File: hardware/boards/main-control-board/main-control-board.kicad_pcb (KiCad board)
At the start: 2 copper layers, 129 x 33 mm, 5 parts

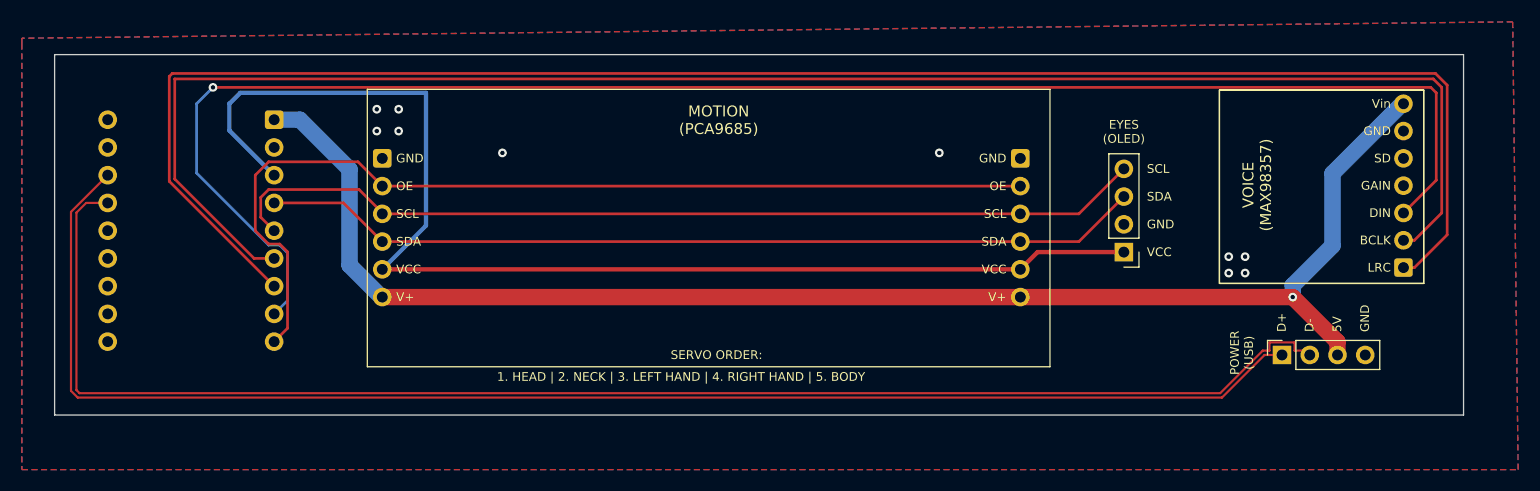
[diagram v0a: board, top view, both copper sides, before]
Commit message: feat(pcb): compact main control board layout and properties
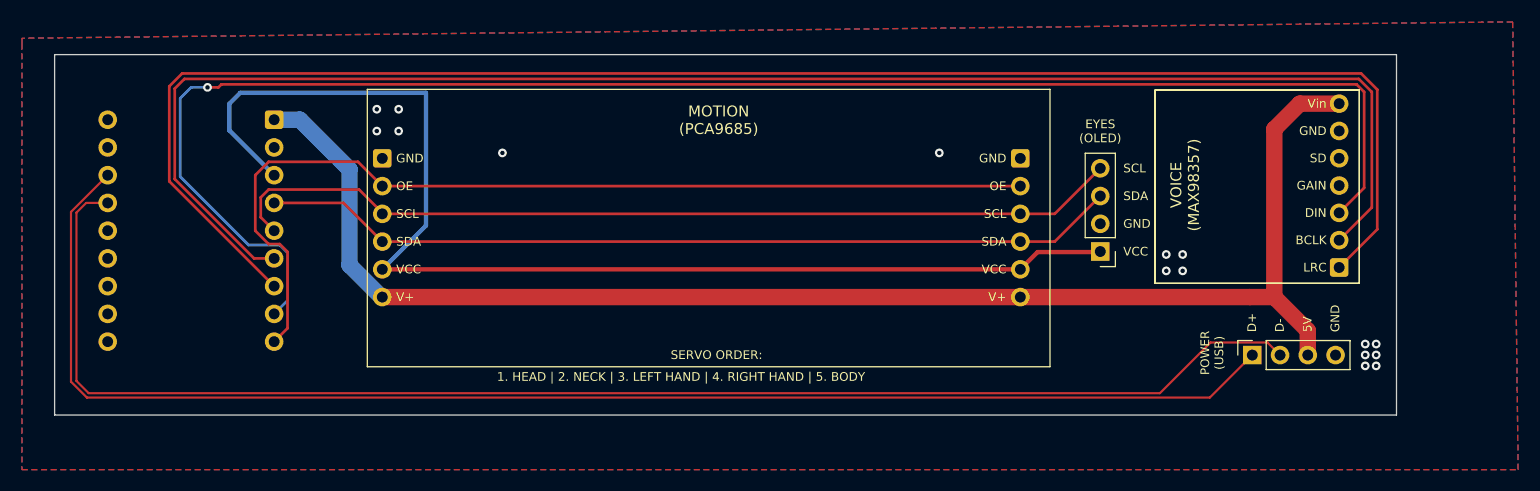
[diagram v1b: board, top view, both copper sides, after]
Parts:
- moved MAX1 5.89 mm to (233.6, 42.0)
- moved USB1 2.72 mm to (233.2, 57.5)
- moved OLED1 2.16 mm to (219.2, 48.0)
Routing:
- net /I2S_LRC: track 159.7 -> 151.7 mm
- net /I2S_BCLK: track 153.6 -> 145.7 mm
- net /USB_D-: track 135.8 -> 131.7 mm
- net /USB_D+: track 133.9 -> 130.7 mm
- net /I2S_DIN: track 150.4 -> 147.2 mm
- net /I2C_SDA: track 81.0 -> 78.8 mm
- net /I2C_SCL: track 85.5 -> 83.4 mm
- net +3.3V: track 113.0 -> 110.9 mm
- net +5V: track 134.0 -> 132.4 mm, vias 1 -> 0
- net GND: vias 10 -> 16
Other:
- board size 129 x 33 mm -> 122.9 x 33 mm

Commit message: prep PCB assembly
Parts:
- MAX1: value MAX98357 -> MAX98357A
- OLED1: value OLED -> Waveshare 0.91 OLED
- PCA1: value PCA9685 -> Adafruit PCA9685
- USB1: value USB -> Conn_01x04_Socket
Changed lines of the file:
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@@
 			)
 		)
-		(property "Value" "PCA9685"
+		(property "Value" "Adafruit PCA9685"
 			(at 0 1 0)
 			(unlocked yes)
@@
 		(sheetname "/")
 		(sheetfile "main-control-board.kicad_sch")
-		(attr through_hole)
+		(units
+			(unit
+				(name "A")
+				(pins "6" "1" "2" "3" "4" "5")
+			)
+		)
+		(attr through_hole exclude_from_pos_files exclude_from_bom)
 		(duplicate_pad_numbers_are_jumpers no)
 		(fp_line
@@
 			(net "/I2C_SCL")
 			(pinfunction "SCL_3")
-			(pintype "bidirectional")
+			(pintype "input")
 		)
 		(pad "3" thru_hole circle
@@
 			(net "/I2C_SCL")
 			(pinfunction "SCL_3")
-			(pintype "bidirectional")
+			(pintype "input")
 		)
 		(pad "4" thru_hole circle
@@
 			)
 		)
-		(property "Value" "USB"
+		(property "Value" "Conn_01x04_Socket"
 			(at -3.15 -0.09 180)
 			(layer "F.Fab")
@@
 			)
 		)
-		(property "Description" ""
+		(property "Description" "Generic connector, single row, 01x04, script generated"
 			(at 0 0 90)
 			(layer "F.Fab")
@@
 			(at 0 0 90)
 			(layer "F.SilkS")
+			(hide yes)
+			(effects
+				(font
+					(size 1 1)
+					(thickness 0.15)
+				)
+			)
+		)
+		(property "LCSC Part #" "C2718488"
+			(at 0 0 90)
+			(unlocked yes)
+			(layer "F.Fab")
+			(hide yes)
+			(effects
+				(font
+					(size 1 1)
+					(thickness 0.15)
+				)
+			)
+		)
+		(property "FT Rotation Offset" "90"
+			(at 0 0 90)
+			(unlocked yes)
+			(layer "F.Fab")
 			(hide yes)
 			(effects
@@
 			)
 		)
-		(property "Value" "MAX98357"
+		(property "Value" "MAX98357A"
 			(at 0 10 180)
 			(unlocked yes)
@@
 		(sheetname "/")
 		(sheetfile "main-control-board.kicad_sch")
-		(attr through_hole)
+		(units
+			(unit
+				(name "A")
+				(pins "1" "2" "3" "4" "5" "7" "6")
+			)
+		)
+		(attr through_hole exclude_from_pos_files exclude_from_bom)
 		(duplicate_pad_numbers_are_jumpers no)
 		(fp_line
@@
 			(net "/I2S_LRC")
 			(pinfunction "LRC_1")
-			(pintype "bidirectional")
+			(pintype "input")
 		)
 		(pad "2" thru_hole circle
@@
 			(net "/I2S_BCLK")
 			(pinfunction "BCLK_2")
-			(pintype "bidirectional")
+			(pintype "input")
 		)
 		(pad "3" thru_hole circle
@@
 			(net "/I2S_DIN")
 			(pinfunction "DIN_3")
-			(pintype "bidirectional")
+			(pintype "input")
 		)
 		(pad "4" thru_hole circle
@@
 			(net "unconnected-(MAX1-GAIN-Pad4)")
 			(pinfunction "GAIN_4")
-			(pintype "bidirectional+no_connect")
+			(pintype "input+no_connect")
 		)
 		(pad "5" thru_hole circle
@@
 			(net "unconnected-(MAX1-SD-Pad5)")
 			(pinfunction "SD_5")
-			(pintype "bidirectional+no_connect")
+			(pintype "input+no_connect")
 		)
 		(pad "6" thru_hole circle
@@
 			)
 		)
-		(property "Value" "OLED"
+		(property "Value" "Waveshare 0.91 OLED"
 			(at 2.65 7.46 90)
 			(layer "F.Fab")
@@
 			(at 0 0 0)
 			(layer "F.SilkS")
+			(hide yes)
+			(effects
+				(font
+					(size 1 1)
+					(thickness 0.15)
+				)
+			)
+		)
+		(property "LCSC Part #" "C2691448"
+			(at 0 0 180)
+			(unlocked yes)
+			(layer "F.Fab")
+			(hide yes)
+			(effects
+				(font
+					(size 1 1)
+					(thickness 0.15)
+				)
+			)
+		)
+		(property "FT Rotation Offset" "90"
+			(at 0 0 180)
+			(unlocked yes)
+			(layer "F.Fab")
 			(hide yes)
 			(effects
@@
 			(net "/I2C_SCL")
 			(pinfunction "SCL_4")
-			(pintype "bidirectional")
+			(pintype "input")
 		)
 		(embedded_fonts no)
@@
 			)
 		)
-		(property "Datasheet" ""
+		(property "Datasheet" "https://www.waveshare.com/wiki/ESP32-C3-Zero"
 			(at 0 0 0)
 			(unlocked yes)
@@
 			)
 		)
-		(property "Description" ""
+		(property "Description" "Waveshare ESP32-C3-Zero module header, pads numbered anticlockwise from USB"
 			(at 0 0 0)
 			(unlocked yes)
@@
 		(sheetname "/")
 		(sheetfile "main-control-board.kicad_sch")
-		(attr through_hole)
+		(units
+			(unit
+				(name "A")
+				(pins "3" "4" "5" "6" "7" "8" "9" "1" "2" "18" "17" "16" "15" "14" "13"
+					"12" "11" "10"
+				)
+			)
+		)
+		(attr through_hole exclude_from_pos_files exclude_from_bom)
 		(duplicate_pad_numbers_are_jumpers no)
 		(fp_line

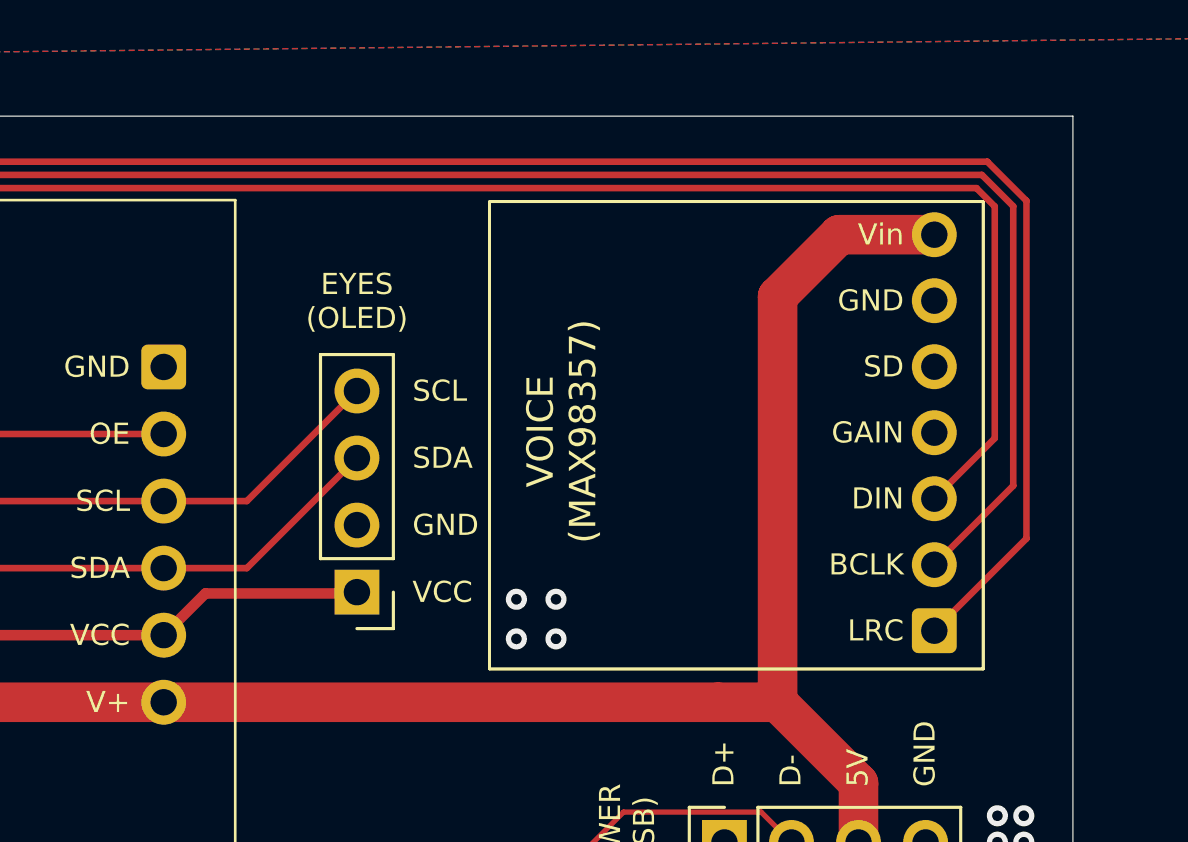
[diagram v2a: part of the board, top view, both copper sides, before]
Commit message: feat(pcb): replace MAX98357 by pin header
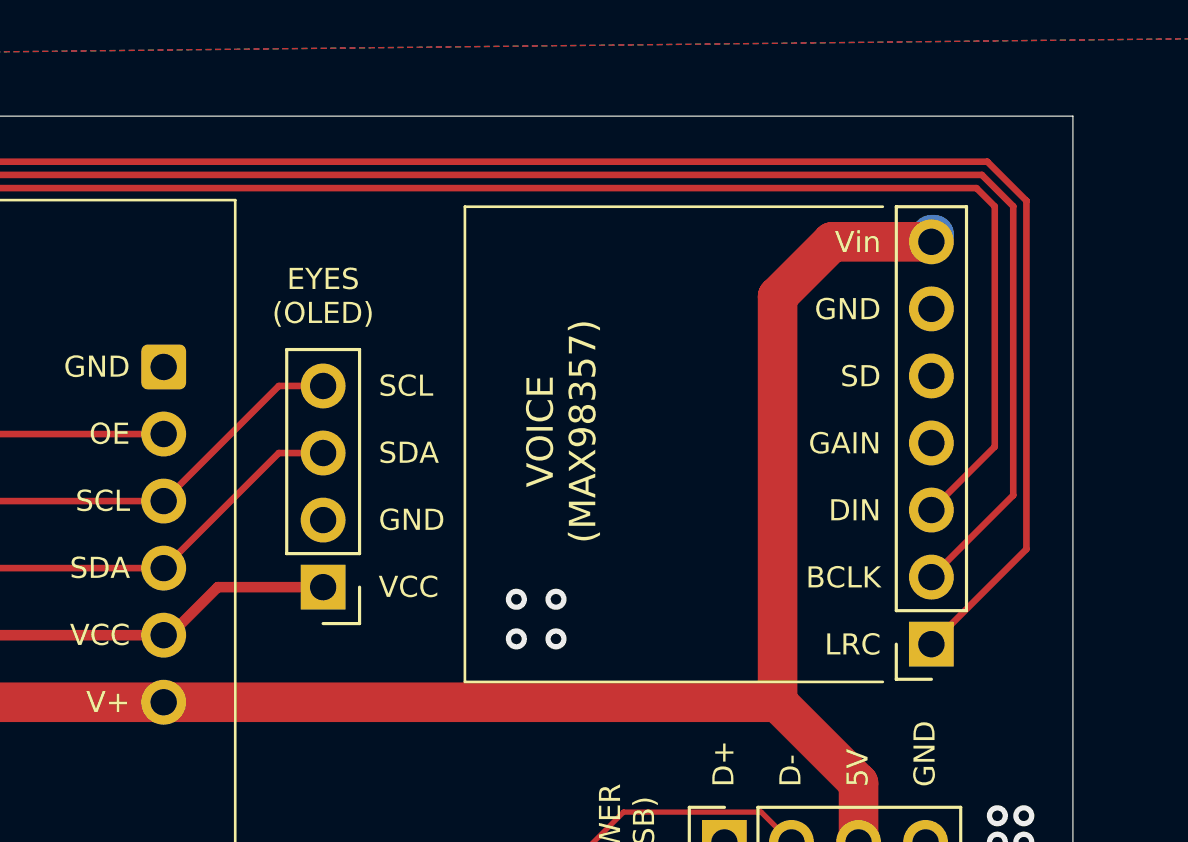
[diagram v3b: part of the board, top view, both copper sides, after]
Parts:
- removed MAX1: MAX98357A, TinyEngineerModules:MAX98357_Module
- added J1: Conn_MAX98357, Connector_PinSocket_2.54mm:PinSocket_1x07_P2.54mm_Vertical, F.Cu at (241.0, 50.0)
- USB1: value Conn_01x04_Socket -> Conn_USB
- moved OLED1 1.29 mm to (218.0, 47.8)
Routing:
- net /I2C_SDA: track 78.8 -> 77.6 mm
- net /I2C_SCL: track 83.4 -> 82.2 mm
- net +3.3V: track 110.9 -> 109.7 mm
- net /I2S_LRC: track 151.7 -> 152.3 mm
- net /I2S_BCLK: track 145.7 -> 146.2 mm
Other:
- board text added: "BCLK"
- board text added: "DIN"
- board text added: "GAIN"
- board text added: "LRC"
- board text added: "SD"
- board text added: "Vin"

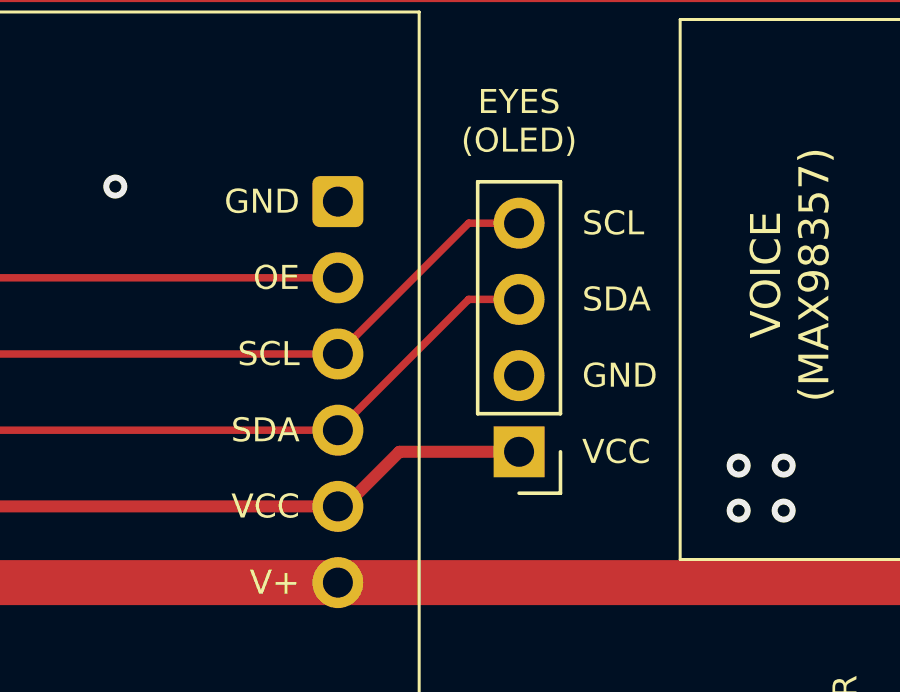
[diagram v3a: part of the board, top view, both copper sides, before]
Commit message: chore(cad): remove custom OLED symbol
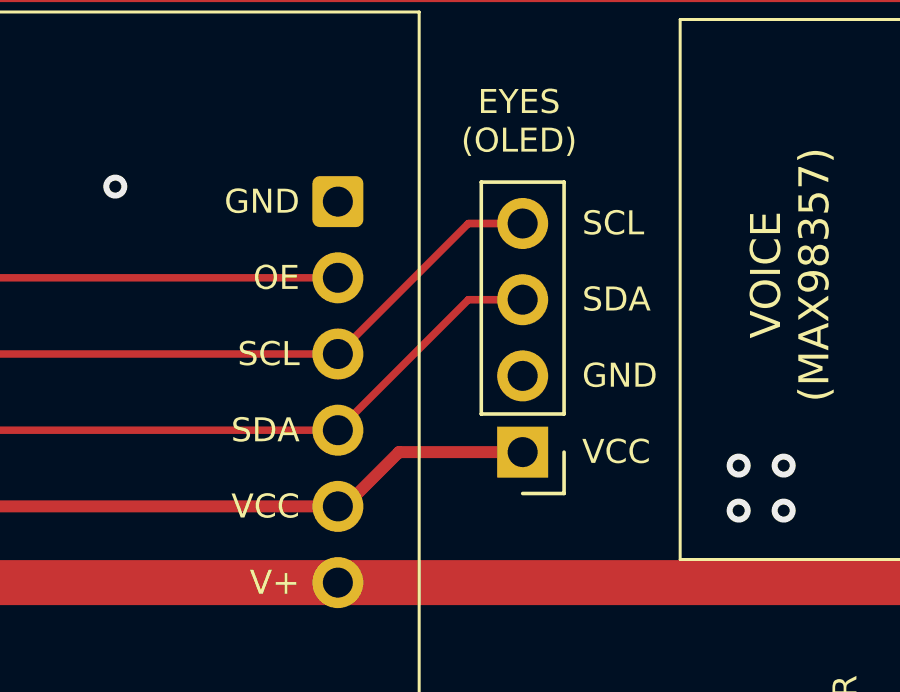
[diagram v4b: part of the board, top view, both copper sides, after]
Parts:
- removed OLED1: Waveshare 0.91 OLED, Connector_PinHeader_2.54mm:PinHeader_1x04_P2.54mm_Vertical
- added J2: Conn_OLED, Connector_PinHeader_2.54mm:PinHeader_1x04_P2.54mm_Vertical, F.Cu at (218.1, 47.9)

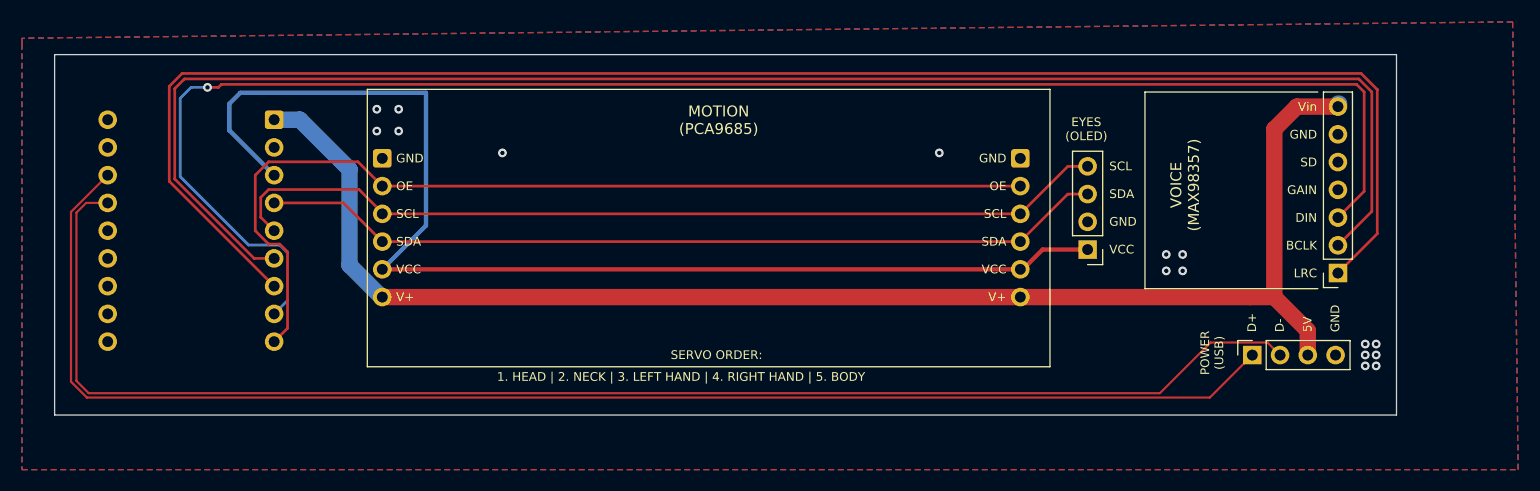
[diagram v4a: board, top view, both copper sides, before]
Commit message: chore(pcb): replace modules by goldpin headers and add headers to BOM
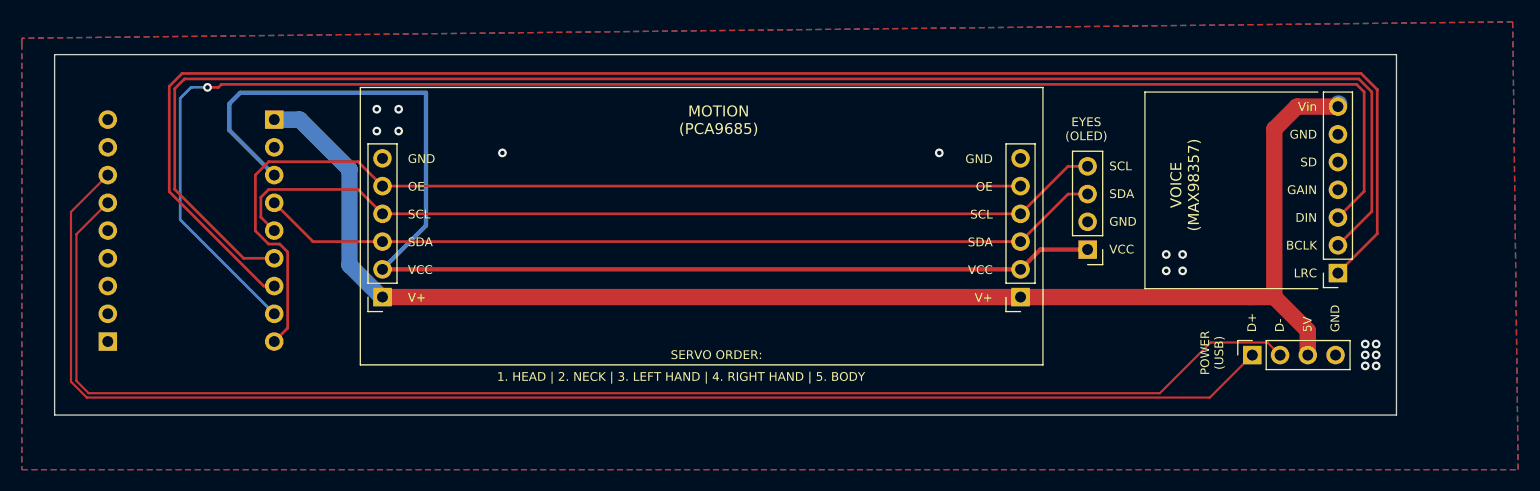
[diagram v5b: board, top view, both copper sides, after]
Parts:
- removed ESP1: ESP32-C3-ZERO, TinyEngineerModules:ESP32_C3_Zero_Dev_Board
- removed PCA1: Adafruit PCA9685, TinyEngineerModules:Adafruit_PCA9685_Module
- added J3: Conn_PCA9685_1, Connector_PinSocket_2.54mm:PinSocket_1x06_P2.54mm_Vertical, F.Cu at (153.5, 52.2)
- added J4: Conn_PCA9685_2, Connector_PinSocket_2.54mm:PinSocket_1x06_P2.54mm_Vertical, F.Cu at (211.9, 52.2)
- added J5: Conn_ESP32_R, Connector_PinSocket_2.54mm:PinSocket_1x09_P2.54mm_Vertical, B.Cu at (128.4, 56.3)
- added J6: Conn_ESP32_L, Connector_PinSocket_2.54mm:PinSocket_1x09_P2.54mm_Vertical, B.Cu at (143.6, 36.0)
- renumbered USB1 to J7
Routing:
- net Net-(J3-Pin_5): track 0.00 -> 89.1 mm
- net Net-(ESP1-GP5): track 89.0 -> 0.00 mm
- net /I2S_DIN: track 147.7 -> 145.0 mm
- net /USB_D-: track 131.7 -> 130.6 mm
- net /I2S_BCLK: track 146.2 -> 146.7 mm
- net /I2S_LRC: track 152.3 -> 152.8 mm
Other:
- board text added: "3V3"
- board text added: "GP0"
- board text added: "GP1"
- board text added: "GP10"
- board text added: "GP2"
- board text added: "GP3"
- board text added: "GP4"
- board text added: "GP5"
- board text added: "GP6"
- board text added: "GP7"
- board text added: "GP8"
- board text added: "GP9"
- board text added: "OE"
- board text added: "RX"
- board text added: "TX"
- board text added: "USB_DM"
- board text added: "USB_DP"
- board text added: "V+"

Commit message: fix(pcb): rotate esp32 headers
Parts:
- moved J5 25.5 mm to (143.6, 35.9), turned to 180 degrees
- moved J6 25.3 mm to (128.4, 56.2), turned to 0 degrees
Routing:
- net /USB_D+: track 130.7 -> 92.2 mm
- net /USB_D-: track 130.6 -> 96.5 mm
- net /I2C_SDA: track 77.8 -> 92.1 mm
- net +5V: track 132.2 -> 145.7 mm
- net /I2S_DIN: track 145.0 -> 133.7 mm, vias 1 -> 0
- net /I2C_SCL: track 82.4 -> 92.2 mm
- net /I2S_BCLK: track 146.7 -> 136.9 mm, vias 0 -> 1
- net +3.3V: track 110.0 -> 101.0 mm
- net /I2S_LRC: track 152.8 -> 145.2 mm
- net Net-(J3-Pin_5): track 89.1 -> 86.1 mm
- net GND: vias 16 -> 14
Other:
- board text added: "USB"
